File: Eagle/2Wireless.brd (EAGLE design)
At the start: 62.7 x 33 mm, 19 parts, among them IC1 TCA9517A, IC3 MB85RS2MTAPNF-G-BDERE1

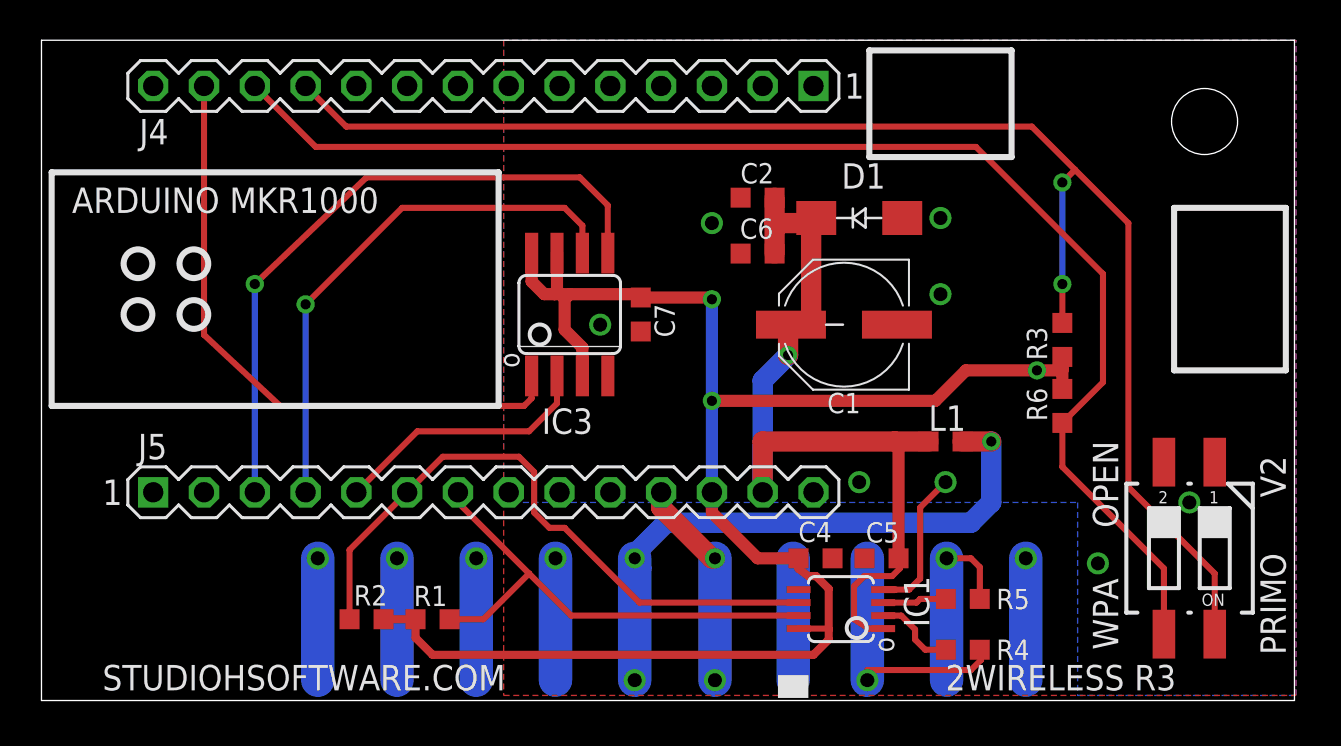
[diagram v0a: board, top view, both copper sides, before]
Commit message: Add blue LED for I2C activity
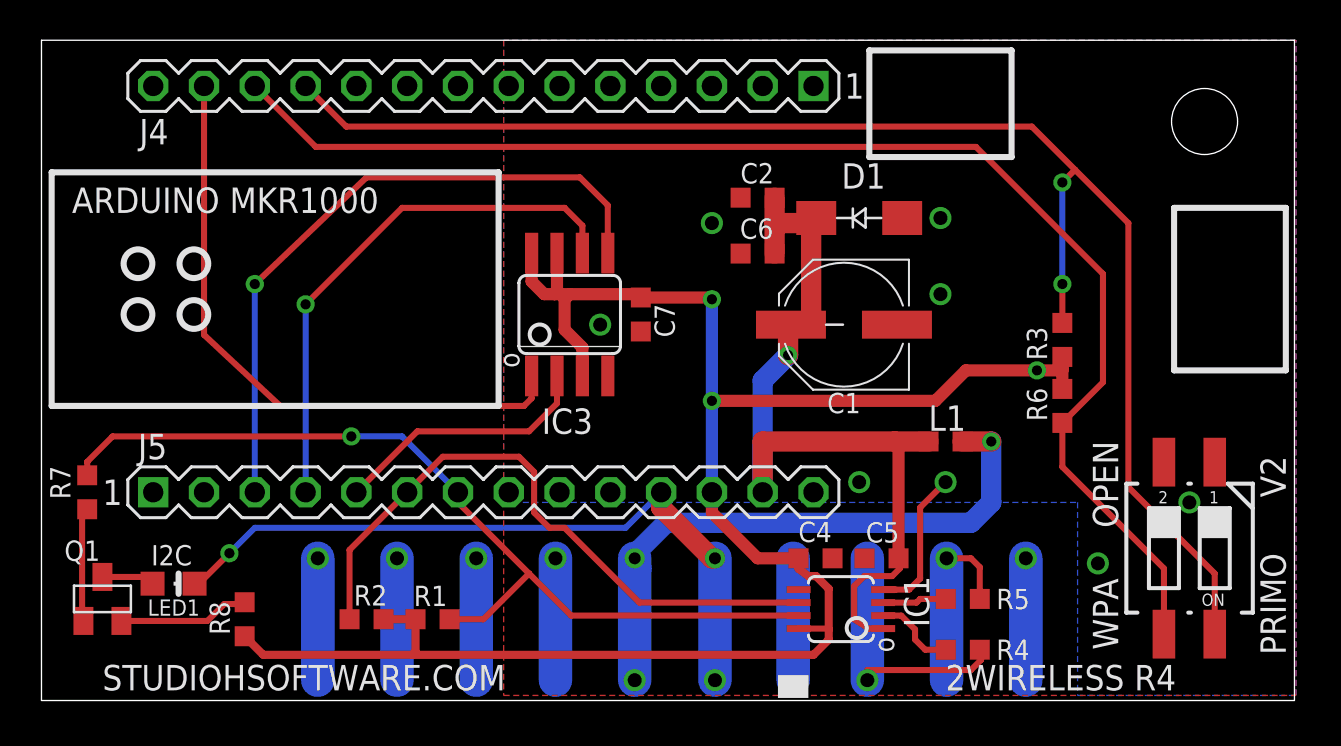
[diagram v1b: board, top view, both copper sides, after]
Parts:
- added LED1: (no value), studio_h:CHIPLED_0805
- added Q1: 2N3906, studio_h:SOT23
- added R7: 1k, studio_h:R0603
- added R8: 0, studio_h:R0603
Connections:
- new net N$1: Q1.1, R7.2
- new net N$2: LED1.A, Q1.2
- new net N$3: Q1.3, R8.1
- net DGND: now also LED1.C
- net DPWR: now also R8.2
- net SCL: now also R7.1
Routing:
- net DGND: track 18.8 -> 44.4 mm, vias 10 -> 11
- net SCL: track 24.8 -> 45.7 mm, vias 0 -> 1
- net DPWR: track 84.9 -> 94.5 mm
- net N$3: track 0.00 -> 6.55 mm
- net N$1: track 0.00 -> 5.72 mm
- net N$2: track 0.00 -> 2.60 mm
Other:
- board text added: "2WIRELESS R4"
- board text added: "I2C"
- board text removed: "2WIRELESS R3"
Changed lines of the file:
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@@
 <wire x1="0" y1="33.02" x2="0" y2="0" width="0.0254" layer="20"/>
 <text x="41.628059375" y="3.175" size="1.016" layer="21" font="vector" ratio="12" rot="R270">o</text>
-<text x="45.212" y="0.508" size="1.27" layer="25" font="vector" ratio="12">2WIRELESS R3</text>
+<text x="45.212" y="0.508" size="1.27" layer="25" font="vector" ratio="12">2WIRELESS R4</text>
 <polygon width="0.3048" layer="30">
 <vertex x="51.308" y="0.254"/>
@@
 <text x="53.848" y="8.636" size="1.27" layer="25" font="vector" ratio="12" rot="R90">OPEN</text>
 <hole x="58.166" y="28.956" drill="3.302"/>
+<text x="5.4864" y="6.7564" size="1.016" layer="25" font="vector" ratio="12">I2C</text>
+<wire x1="6.858" y1="6.35" x2="6.858" y2="5.334" width="0.3048" layer="21"/>
 </plain>
 <attributes>
@@
 <attribute name="VALUE" x="15.621" y="2.084" size="1.016" layer="27" font="vector" ratio="12"/>
 </element>
+<element name="Q1" library="studio_h" package="SOT23" value="2N3906" x="3.048" y="5.08">
+<attribute name="MPN" value="MMBT3906" x="3.048" y="5.08" size="1.778" layer="27" display="off"/>
+<attribute name="MF" value="FAIRCHILD" x="3.048" y="5.08" size="1.778" layer="27" display="off"/>
+<attribute name="Z_DIGIKEY" value="MMBT3906FSCT-ND" x="3.048" y="5.08" size="1.778" layer="27" display="off"/>
+<attribute name="Z_SMT" value="Y" x="3.048" y="5.08" size="1.778" layer="27" display="off"/>
+<attribute name="Z_MOUSER" value="512-MMBT3906" x="3.048" y="5.08" size="1.778" layer="27" display="off"/>
+</element>
+<element name="R7" library="studio_h" package="R0603" value="1k" x="2.286" y="10.414" smashed="yes" rot="R270">
+<attribute name="Z_SMT" value="Y" x="2.286" y="10.414" size="1.778" layer="27" rot="R270" display="off"/>
+<attribute name="NAME" x="0.431" y="11.7348" size="1.016" layer="25" font="vector" ratio="12" rot="R270"/>
+<attribute name="VALUE" x="0.306" y="11.049" size="1.016" layer="27" font="vector" ratio="12" rot="R270"/>
+</element>
+<element name="R8" library="studio_h" package="R0603" value="0" x="10.16" y="4.064" smashed="yes" rot="R270">
+<attribute name="Z_SMT" value="Y" x="10.16" y="4.064" size="1.778" layer="27" rot="R270" display="off"/>
+<attribute name="NAME" x="8.4066" y="4.953" size="1.016" layer="25" font="vector" ratio="12" rot="R270"/>
+<attribute name="VALUE" x="8.18" y="4.699" size="1.016" layer="27" font="vector" ratio="12" rot="R270"/>
+</element>
+<element name="LED1" library="studio_h" package="CHIPLED_0805" value="" x="6.604" y="5.842" smashed="yes" rot="R270">
+<attribute name="NAME" x="5.3086" y="4.2418" size="0.8128" layer="25" font="vector" ratio="12"/>
+<attribute name="VALUE" x="5.969" y="3.937" size="1.27" layer="27"/>
+</element>
 </elements>
 <signals>
@@
 <wire x1="20.408" y1="4.064" x2="22.098" y2="4.064" width="0.3048" layer="1"/>
 <wire x1="22.098" y1="4.064" x2="24.384" y2="6.35" width="0.3048" layer="1"/>
+<contactref element="R7" pad="1"/>
+<via x="15.494" y="13.208" extent="1-16" drill="0.508"/>
+<wire x1="15.494" y1="13.208" x2="18.034" y2="13.208" width="0.3048" layer="16"/>
+<wire x1="18.034" y1="13.208" x2="20.828" y2="10.414" width="0.3048" layer="16"/>
+<wire x1="2.286" y1="11.264" x2="2.286" y2="11.938" width="0.3048" layer="1"/>
+<wire x1="2.286" y1="11.938" x2="3.556" y2="13.208" width="0.3048" layer="1"/>
+<wire x1="3.556" y1="13.208" x2="15.494" y2="13.208" width="0.3048" layer="1"/>
 </signal>
 <signal name="SDA">
@@
 <wire x1="43.942" y1="6.096" x2="43.942" y2="9.652" width="0.3048" layer="1"/>
 <wire x1="43.942" y1="9.652" x2="45.212" y2="10.922" width="0.3048" layer="1"/>
+<contactref element="LED1" pad="C"/>
+<via x="9.398" y="7.366" extent="1-16" drill="0.508"/>
+<wire x1="9.398" y1="7.366" x2="10.668" y2="8.636" width="0.3048" layer="16"/>
+<wire x1="10.668" y1="8.636" x2="29.21" y2="8.636" width="0.3048" layer="16"/>
+<wire x1="29.21" y1="8.636" x2="30.988" y2="10.414" width="0.3048" layer="16"/>
+<wire x1="7.654" y1="5.842" x2="7.62" y2="5.588" width="0.3048" layer="1"/>
+<wire x1="7.62" y1="5.588" x2="9.398" y2="7.366" width="0.3048" layer="1"/>
 </signal>
 <signal name="EDAC-12V+">
@@
 <wire x1="39.37" y1="3.556" x2="39.37" y2="3.048" width="0.4064" layer="1"/>
 <wire x1="39.37" y1="3.048" x2="38.608" y2="2.286" width="0.4064" layer="1"/>
-<wire x1="38.608" y1="2.286" x2="19.558" y2="2.286" width="0.4064" layer="1"/>
-<wire x1="19.558" y1="2.286" x2="18.708" y2="3.136" width="0.4064" layer="1"/>
+<wire x1="38.608" y1="2.286" x2="18.542" y2="2.286" width="0.4064" layer="1"/>
+<wire x1="18.542" y1="2.286" x2="11.088" y2="2.286" width="0.4064" layer="1"/>
 <wire x1="17.106" y1="4.064" x2="18.708" y2="4.064" width="0.4064" layer="1"/>
-<wire x1="18.708" y1="4.064" x2="18.708" y2="3.136" width="0.4064" layer="1"/>
 <wire x1="37.8676" y1="3.596" x2="39.33" y2="3.596" width="0.3048" layer="1"/>
 <wire x1="39.33" y1="3.596" x2="39.37" y2="3.556" width="0.3048" layer="1"/>
+<contactref element="R8" pad="2"/>
+<wire x1="17.018" y1="3.976" x2="17.106" y2="4.064" width="0.3048" layer="1"/>
+<wire x1="11.088" y1="2.286" x2="10.16" y2="3.214" width="0.4064" layer="1"/>
+<wire x1="18.708" y1="4.064" x2="18.708" y2="2.452" width="0.4064" layer="1"/>
+<wire x1="18.708" y1="2.452" x2="18.542" y2="2.286" width="0.4064" layer="1"/>
 </signal>
 <signal name="DI-VERSION">
@@
 <wire x1="51.054" y1="11.684" x2="51.054" y2="13.882" width="0.3048" layer="1"/>
 </signal>
+<signal name="N$1">
+<contactref element="Q1" pad="1"/>
+<contactref element="R7" pad="2"/>
+<wire x1="2.032" y1="4.046" x2="2.098" y2="3.98" width="0.3048" layer="1"/>
+<wire x1="2.032" y1="4.046" x2="2.032" y2="9.31" width="0.3048" layer="1"/>
+<wire x1="2.032" y1="9.31" x2="2.286" y2="9.564" width="0.3048" layer="1"/>
+</signal>
+<signal name="N$2">
+<contactref element="Q1" pad="2"/>
+<contactref element="LED1" pad="A"/>
+<wire x1="3.048" y1="6.18" x2="5.008" y2="6.18" width="0.3048" layer="1"/>
+<wire x1="5.008" y1="6.18" x2="5.554" y2="5.842" width="0.3048" layer="1"/>
+</signal>
+<signal name="N$3">
+<contactref element="R8" pad="1"/>
+<contactref element="Q1" pad="3"/>
+<wire x1="3.998" y1="3.98" x2="8.298" y2="3.98" width="0.3048" layer="1"/>
+<wire x1="8.298" y1="3.98" x2="9.144" y2="4.826" width="0.3048" layer="1"/>
+<wire x1="9.144" y1="4.826" x2="10.072" y2="4.826" width="0.3048" layer="1"/>
+<wire x1="10.072" y1="4.826" x2="10.16" y2="4.914" width="0.3048" layer="1"/>
+</signal>
 </signals>
